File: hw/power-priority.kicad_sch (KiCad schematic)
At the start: 12 parts, among them IC1801 LM74800QDRRRQ1, Q1801 IPB026N06NATMA1, Q2307 IPB026N06NATMA1, Q2308 IPB026N06NATMA1, Q2309 2N7002, U2304 LM74700QDRQ1

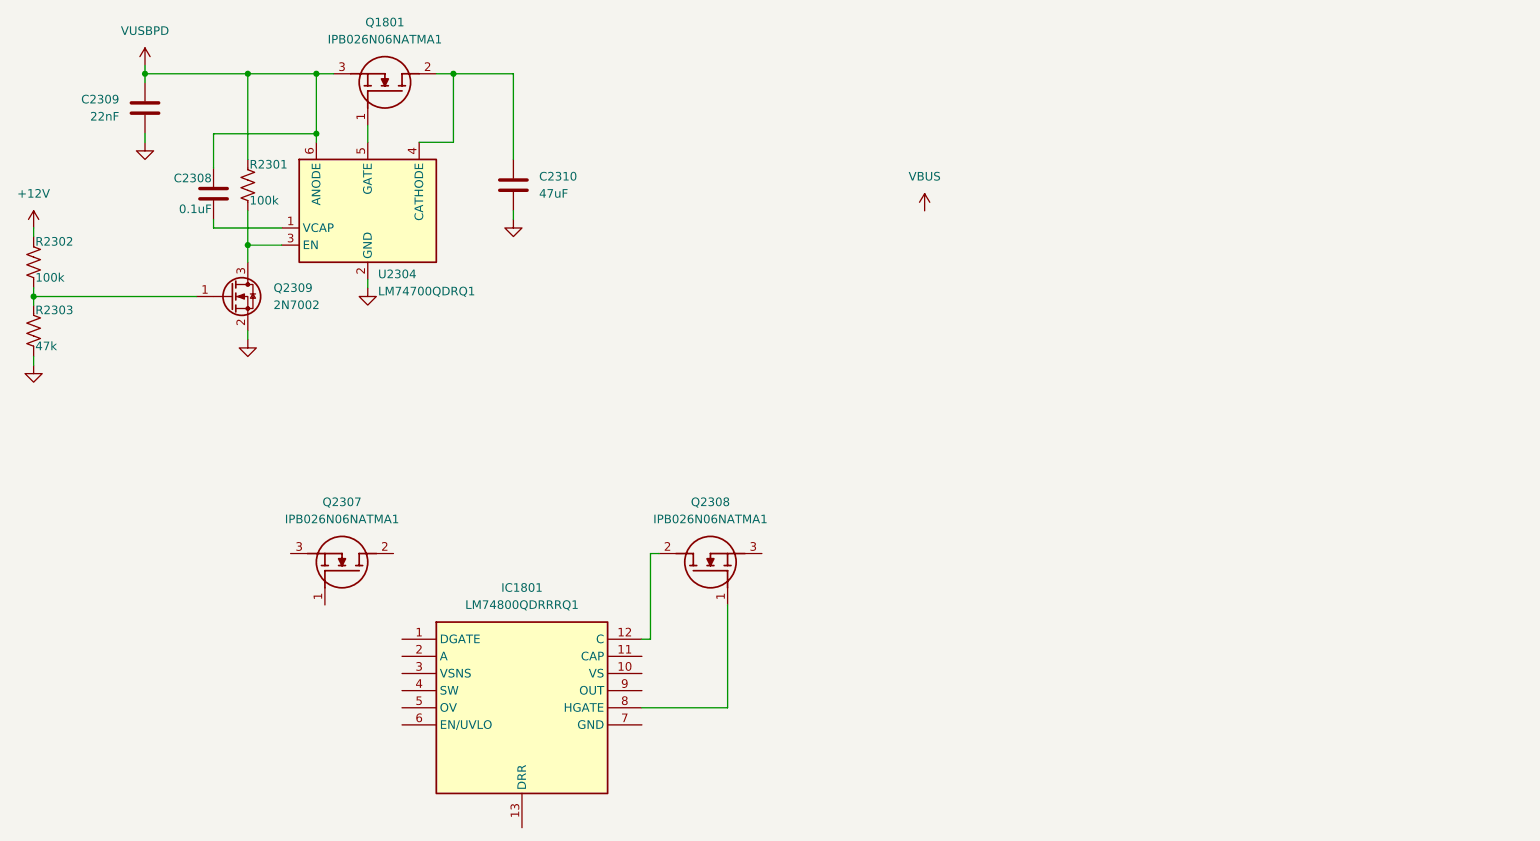
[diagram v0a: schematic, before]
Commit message: Schematic capture of the USBPD and +12V (+12V has priority) power scheme is "done". Have started working on RF deck mezzanine module but not yet divorced into another project
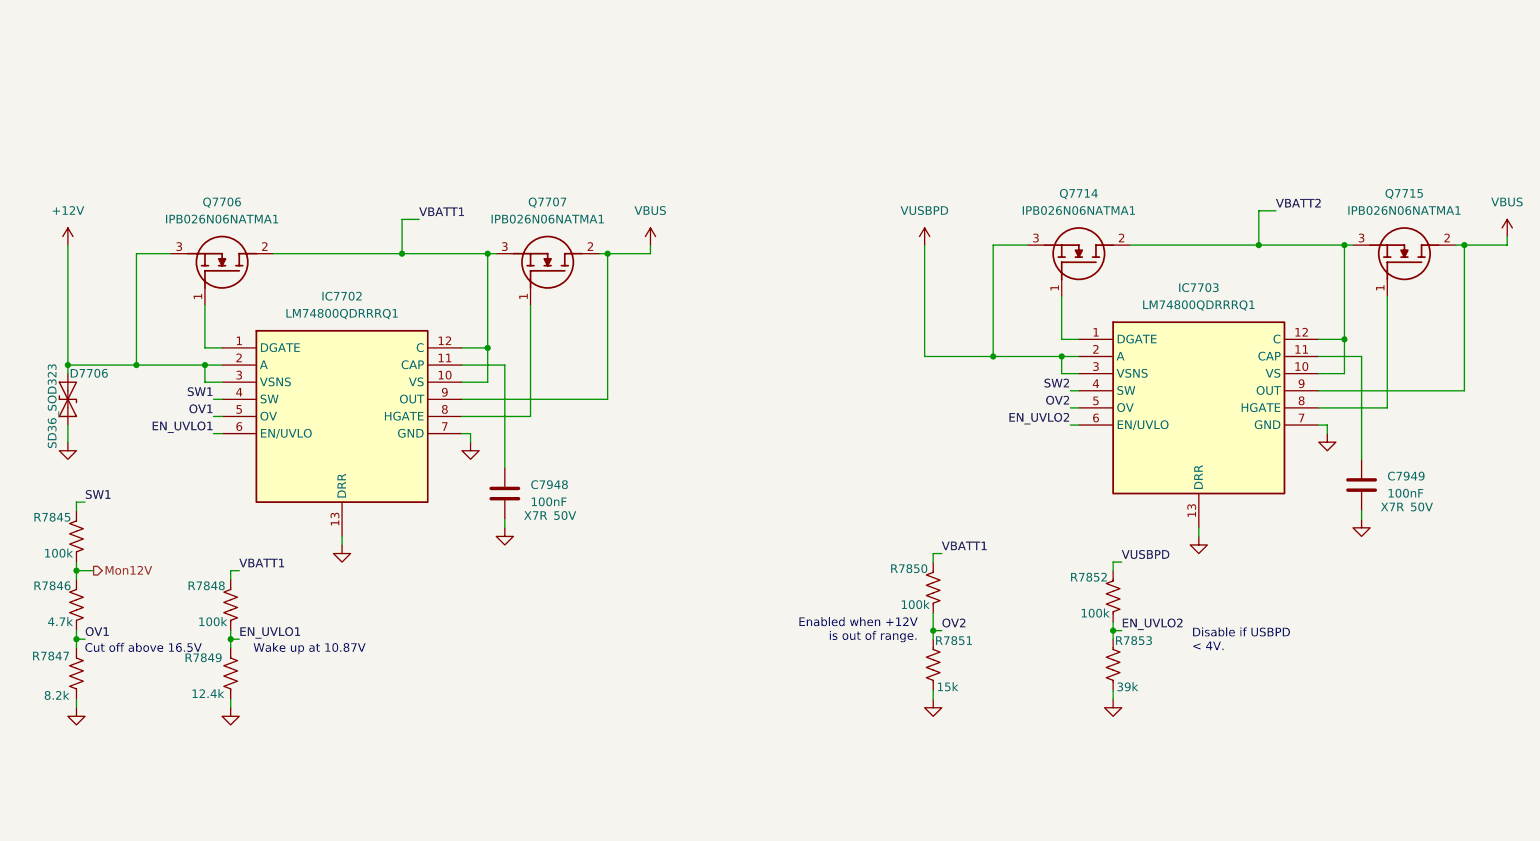
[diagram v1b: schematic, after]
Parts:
- removed C2308: 0.1uF, symbol Device:C
- removed C2309: 22nF, symbol Device:C
- removed C2310: 47uF, symbol Device:C
- removed Q1801, Q2308: IPB026N06NATMA1, IPB026N06NATMA1, symbol Library:IPB026N06NATMA1
- removed Q2309: 2N7002, Package_TO_SOT_SMD:SOT-23, symbol Transistor_FET:2N7002
- removed R2301, R2302: 100k, symbol Device:R_US
- removed R2303: 47k, symbol Device:R_US
- removed U2304: LM74700QDRQ1, Package_TO_SOT_SMD:SOT-23-6, symbol Power_Management:LM74700
- added C7948, C7949: 100nF, symbol Device:C
- added D7706: SD36_SOD323, Diode_SMD:D_SOD-323, symbol Diode:SD36_SOD323
- added IC7703: LM74800QDRRRQ1, SON50P300X300X80-13N, symbol Library:LM74800QDRRRQ1
- added Q7707, Q7714, Q7715: IPB026N06NATMA1, IPB026N06NATMA1, symbol Library:IPB026N06NATMA1
- added R7845, R7848, R7850, R7852: 100k, symbol Device:R_US
- added R7846: 4.7k, symbol Device:R_US
- added R7847: 8.2k, symbol Device:R_US
- added R7849: 12.4k, symbol Device:R_US
- added R7851: 15k, symbol Device:R_US
- added R7853: 39k, symbol Device:R_US
- renumbered IC1801 to IC7702, Q2307 to Q7706
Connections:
- net +12V: now also IC7702.2 (A), IC7702.3 (VSNS), Q7706.3 (S), D7706.2 (A2)
- net GND: now also IC7702.13 (DRR), IC7702.7 (GND), C7948.2, C7949.2, D7706.1 (A1), IC7703.13 (DRR), IC7703.7 (GND), R7847.2, R7849.2, R7851.2, R7853.2
- net VBUS: now also IC7702.9 (OUT), IC7703.9 (OUT), Q7707.2 (D), Q7715.2 (D)
- net VUSBPD: now also IC7703.2 (A), IC7703.3 (VSNS), Q7714.3 (S), R7852.1
- net at IC7702.8 (HGATE): now also Q7707.1 (G)
- net VBATT1: now reaches IC7702.12 (C)
- net VBATT1: now also IC7702.10 (VS), Q7706.2 (D), Q7707.3 (S), R7848.1, R7850.1
- net at IC7702.1 (DGATE): now also Q7706.1 (G)
- net at IC7702.11 (CAP): now also C7948.1
- net SW1: now reaches IC7702.4 (SW)
- net SW1: now also R7845.1
- net OV1: now reaches IC7702.5 (OV)
- net OV1: now also R7846.2, R7847.1
- net EN_UVLO1: now reaches IC7702.6 (EN/UVLO)
- net EN_UVLO1: now also R7848.2, R7849.1
- new net: IC7703.1 (DGATE), Q7714.1 (G)
- new net: C7949.1, IC7703.11 (CAP)
- new net: IC7703.8 (HGATE), Q7715.1 (G)
- new net EN_UVLO2: IC7703.6 (EN/UVLO), R7852.2, R7853.1
- new net Mon12V: R7845.2, R7846.1
- new net OV2: IC7703.5 (OV), R7850.2, R7851.1
- new net SW2: IC7703.4 (SW)
- new net VBATT2: IC7703.10 (VS), IC7703.12 (C), Q7714.2 (D), Q7715.3 (S)
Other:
- note added: "Cut off above 16.5V"
- note added: "Disable if USBPD < 4V."
- note added: "Enabled when +12V is out of range."
- note added: "Wake up at 10.87V"
- moved on the sheet: IC7702, Q7706

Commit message: Last rites for 800 ohm rx preselector, and probably the RF deck which was stillborn
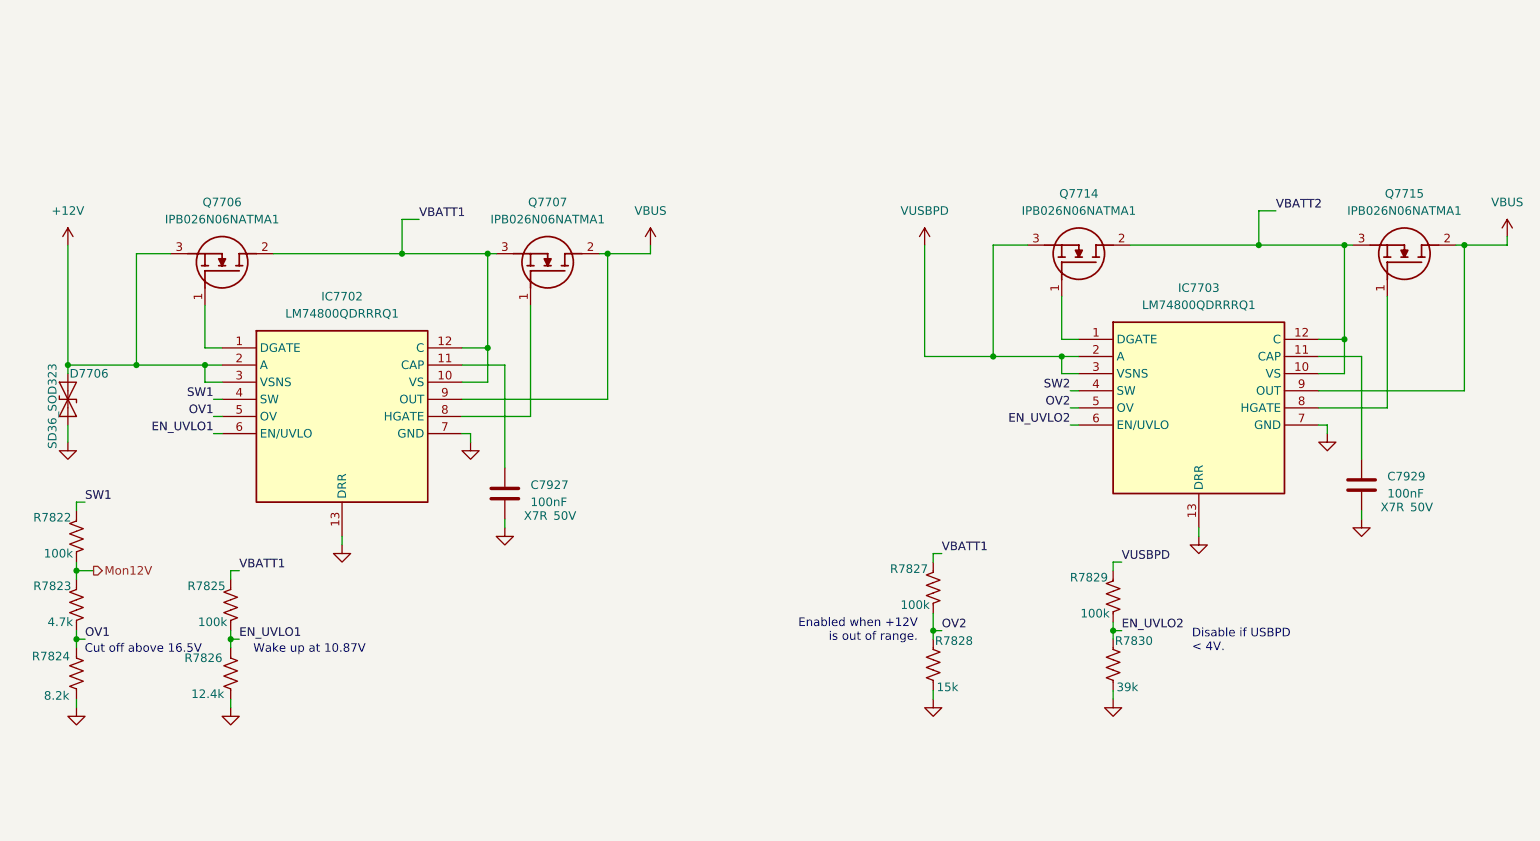
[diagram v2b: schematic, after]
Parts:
- renumbered C7948 to C7927, C7949 to C7929, R7845 to R7822, R7846 to R7823, R7847 to R7824, R7848 to R7825, R7849 to R7826, R7850 to R7827, R7851 to R7828, R7852 to R7829, R7853 to R7830
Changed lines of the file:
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@@
 	(title_block
 		(title "Power Priority Switching")
-		(date "2025-11-21")
+		(date "2025-10-13")
 		(company "WB7NAB")
 		(comment 1 "Alan Mimms")
@@
 		(dnp no)
 		(fields_autoplaced yes)
-		(property "Reference" "#PWR08038"
+		(property "Reference" "#PWR07982"
 			(at 127 72.39 0)
 			(effects
@@
 			(project "NexRig"
 				(path "/8ae46c04-d01a-4756-8774-512b694bfaff/cbf7569b-90aa-4e1a-84a7-d4153f6242b6/b06410ec-4c8e-4291-9691-3a63bcaba95c"
-					(reference "#PWR08038")
+					(reference "#PWR07982")
 					(unit 1)
 				)
@@
 		(dnp no)
 		(fields_autoplaced yes)
-		(property "Reference" "#PWR08034"
+		(property "Reference" "#PWR07978"
 			(at 100.33 104.14 0)
 			(effects
@@
 			(project "NexRig"
 				(path "/8ae46c04-d01a-4756-8774-512b694bfaff/cbf7569b-90aa-4e1a-84a7-d4153f6242b6/b06410ec-4c8e-4291-9691-3a63bcaba95c"
-					(reference "#PWR08034")
+					(reference "#PWR07978")
 					(unit 1)
 				)
@@
 		(on_board yes)
 		(dnp no)
-		(property "Reference" "R7853"
+		(property "Reference" "R7830"
 			(at 195.834 127.254 0)
 			(effects
@@
 			(project "NexRig"
 				(path "/8ae46c04-d01a-4756-8774-512b694bfaff/cbf7569b-90aa-4e1a-84a7-d4153f6242b6/b06410ec-4c8e-4291-9691-3a63bcaba95c"
-					(reference "R7853")
+					(reference "R7830")
 					(unit 1)
 				)
@@
 		(dnp no)
 		(fields_autoplaced yes)
-		(property "Reference" "#PWR08025"
+		(property "Reference" "#PWR07969"
 			(at 40.64 72.39 0)
 			(effects
@@
 			(project "NexRig"
 				(path "/8ae46c04-d01a-4756-8774-512b694bfaff/cbf7569b-90aa-4e1a-84a7-d4153f6242b6/b06410ec-4c8e-4291-9691-3a63bcaba95c"
-					(reference "#PWR08025")
+					(reference "#PWR07969")
 					(unit 1)
 				)
@@
 		(on_board yes)
 		(dnp no)
-		(property "Reference" "R7847"
+		(property "Reference" "R7824"
 			(at 35.306 129.54 0)
 			(effects
@@
 			(project ""
 				(path "/8ae46c04-d01a-4756-8774-512b694bfaff/cbf7569b-90aa-4e1a-84a7-d4153f6242b6/b06410ec-4c8e-4291-9691-3a63bcaba95c"
-					(reference "R7847")
+					(reference "R7824")
 					(unit 1)
 				)
@@
 		(dnp no)
 		(fields_autoplaced yes)
-		(property "Reference" "#PWR08043"
+		(property "Reference" "#PWR07987"
 			(at 167.64 72.39 0)
 			(effects
@@
 			(project "NexRig"
 				(path "/8ae46c04-d01a-4756-8774-512b694bfaff/cbf7569b-90aa-4e1a-84a7-d4153f6242b6/b06410ec-4c8e-4291-9691-3a63bcaba95c"
-					(reference "#PWR08043")
+					(reference "#PWR07987")
 					(unit 1)
 				)
@@
 		(on_board yes)
 		(dnp no)
-		(property "Reference" "R7848"
+		(property "Reference" "R7825"
 			(at 64.008 119.126 0)
 			(effects
@@
 			(project "NexRig"
 				(path "/8ae46c04-d01a-4756-8774-512b694bfaff/cbf7569b-90aa-4e1a-84a7-d4153f6242b6/b06410ec-4c8e-4291-9691-3a63bcaba95c"
-					(reference "R7848")
+					(reference "R7825")
 					(unit 1)
 				)
@@
 		(on_board yes)
 		(dnp no)
-		(property "Reference" "R7845"
+		(property "Reference" "R7822"
 			(at 41.148 108.966 0)
 			(effects
@@
 			(project "NexRig"
 				(path "/8ae46c04-d01a-4756-8774-512b694bfaff/cbf7569b-90aa-4e1a-84a7-d4153f6242b6/b06410ec-4c8e-4291-9691-3a63bcaba95c"
-					(reference "R7845")
+					(reference "R7822")
 					(unit 1)
 				)
@@
 		(on_board yes)
 		(dnp no)
-		(property "Reference" "R7850"
+		(property "Reference" "R7827"
 			(at 168.148 116.586 0)
 			(effects
@@
 			(project "NexRig"
 				(path "/8ae46c04-d01a-4756-8774-512b694bfaff/cbf7569b-90aa-4e1a-84a7-d4153f6242b6/b06410ec-4c8e-4291-9691-3a63bcaba95c"
-					(reference "R7850")
+					(reference "R7827")
 					(unit 1)
 				)
@@
 		(dnp no)
 		(fields_autoplaced yes)
-		(property "Reference" "#PWR08031"
+		(property "Reference" "#PWR07975"
 			(at 81.28 119.38 0)
 			(effects
@@
 			(project "NexRig"
 				(path "/8ae46c04-d01a-4756-8774-512b694bfaff/cbf7569b-90aa-4e1a-84a7-d4153f6242b6/b06410ec-4c8e-4291-9691-3a63bcaba95c"
-					(reference "#PWR08031")
+					(reference "#PWR07975")
 					(unit 1)
 				)
@@
 		(on_board yes)
 		(dnp no)
-		(property "Reference" "R7849"
+		(property "Reference" "R7826"
 			(at 57.912 129.794 0)
 			(effects
@@
 			(project "NexRig"
 				(path "/8ae46c04-d01a-4756-8774-512b694bfaff/cbf7569b-90aa-4e1a-84a7-d4153f6242b6/b06410ec-4c8e-4291-9691-3a63bcaba95c"
-					(reference "R7849")
+					(reference "R7826")
 					(unit 1)
 				)
@@
 		(dnp no)
 		(fields_autoplaced yes)
-		(property "Reference" "#PWR08051"
+		(property "Reference" "#PWR07994"
 			(at 227.33 102.87 0)
 			(effects
@@
 			(project "NexRig"
 				(path "/8ae46c04-d01a-4756-8774-512b694bfaff/cbf7569b-90aa-4e1a-84a7-d4153f6242b6/b06410ec-4c8e-4291-9691-3a63bcaba95c"
-					(reference "#PWR08051")
+					(reference "#PWR07994")
 					(unit 1)
 				)
@@
 		(dnp no)
 		(fields_autoplaced yes)
-		(property "Reference" "#PWR08047"
+		(property "Reference" "#PWR07991"
 			(at 208.28 118.11 0)
 			(effects
@@
 			(project "NexRig"
 				(path "/8ae46c04-d01a-4756-8774-512b694bfaff/cbf7569b-90aa-4e1a-84a7-d4153f6242b6/b06410ec-4c8e-4291-9691-3a63bcaba95c"
-					(reference "#PWR08047")
+					(reference "#PWR07991")
 					(unit 1)
 				)
@@
 		(dnp no)
 		(fields_autoplaced yes)
-		(property "Reference" "#PWR08026"
+		(property "Reference" "#PWR07970"
 			(at 40.64 104.14 0)
 			(effects
@@
 			(project "NexRig"
 				(path "/8ae46c04-d01a-4756-8774-512b694bfaff/cbf7569b-90aa-4e1a-84a7-d4153f6242b6/b06410ec-4c8e-4291-9691-3a63bcaba95c"
-					(reference "#PWR08026")
+					(reference "#PWR07970")
 					(unit 1)
 				)
@@
 		(on_board yes)
 		(dnp no)
-		(property "Reference" "R7852"
+		(property "Reference" "R7829"
 			(at 194.818 117.856 0)
 			(effects
@@
 			(project "NexRig"
 				(path "/8ae46c04-d01a-4756-8774-512b694bfaff/cbf7569b-90aa-4e1a-84a7-d4153f6242b6/b06410ec-4c8e-4291-9691-3a63bcaba95c"
-					(reference "R7852")
+					(reference "R7829")
 					(unit 1)
 				)
@@
 		(dnp no)
 		(fields_autoplaced yes)
-		(property "Reference" "#PWR08028"
+		(property "Reference" "#PWR07972"
 			(at 41.91 143.51 0)
 			(effects
@@
 			(project "NexRig"
 				(path "/8ae46c04-d01a-4756-8774-512b694bfaff/cbf7569b-90aa-4e1a-84a7-d4153f6242b6/b06410ec-4c8e-4291-9691-3a63bcaba95c"
-					(reference "#PWR08028")
+					(reference "#PWR07972")
 					(unit 1)
 				)
@@
 		(dnp no)
 		(fields_autoplaced yes)
-		(property "Reference" "#PWR08052"
+		(property "Reference" "#PWR07995"
 			(at 232.41 115.57 0)
 			(effects
@@
 			(project "NexRig"
 				(path "/8ae46c04-d01a-4756-8774-512b694bfaff/cbf7569b-90aa-4e1a-84a7-d4153f6242b6/b06410ec-4c8e-4291-9691-3a63bcaba95c"
-					(reference "#PWR08052")
+					(reference "#PWR07995")
 					(unit 1)
 				)
@@
 		(on_board yes)
 		(dnp no)
-		(property "Reference" "C7949"
+		(property "Reference" "C7929"
 			(at 236.22 102.8699 0)
 			(effects
@@
 			(project "NexRig"
 				(path "/8ae46c04-d01a-4756-8774-512b694bfaff/cbf7569b-90aa-4e1a-84a7-d4153f6242b6/b06410ec-4c8e-4291-9691-3a63bcaba95c"
-					(reference "C7949")
+					(reference "C7929")
 					(unit 1)
 				)
@@
 		(dnp no)
 		(fields_autoplaced yes)
-		(property "Reference" "#PWR08030"
+		(property "Reference" "#PWR07974"
 			(at 64.77 143.51 0)
 			(effects
@@
 			(project "NexRig"
 				(path "/8ae46c04-d01a-4756-8774-512b694bfaff/cbf7569b-90aa-4e1a-84a7-d4153f6242b6/b06410ec-4c8e-4291-9691-3a63bcaba95c"
-					(reference "#PWR08030")
+					(reference "#PWR07974")
 					(unit 1)
 				)
@@
 		(dnp no)
 		(fields_autoplaced yes)
-		(property "Reference" "#PWR08054"
+		(property "Reference" "#PWR07998"
 			(at 254 71.12 0)
 			(effects
@@
 			(project "NexRig"
 				(path "/8ae46c04-d01a-4756-8774-512b694bfaff/cbf7569b-90aa-4e1a-84a7-d4153f6242b6/b06410ec-4c8e-4291-9691-3a63bcaba95c"
-					(reference "#PWR08054")
+					(reference "#PWR07998")
 					(unit 1)
 				)
@@
 		(dnp no)
 		(fields_autoplaced yes)
-		(property "Reference" "#PWR08035"
+		(property "Reference" "#PWR07979"
 			(at 105.41 116.84 0)
 			(effects
@@
 			(project "NexRig"
 				(path "/8ae46c04-d01a-4756-8774-512b694bfaff/cbf7569b-90aa-4e1a-84a7-d4153f6242b6/b06410ec-4c8e-4291-9691-3a63bcaba95c"
-					(reference "#PWR08035")
+					(reference "#PWR07979")
 					(unit 1)
 				)
@@
 		(dnp no)
 		(fields_autoplaced yes)
-		(property "Reference" "#PWR08046"
+		(property "Reference" "#PWR07990"
 			(at 195.58 142.24 0)
 			(effects
@@
 			(project "NexRig"
 				(path "/8ae46c04-d01a-4756-8774-512b694bfaff/cbf7569b-90aa-4e1a-84a7-d4153f6242b6/b06410ec-4c8e-4291-9691-3a63bcaba95c"
-					(reference "#PWR08046")
+					(reference "#PWR07990")
 					(unit 1)
 				)
@@
 		(on_board yes)
 		(dnp no)
-		(property "Reference" "R7851"
+		(property "Reference" "R7828"
 			(at 169.164 127.254 0)
 			(effects
@@
 			(project "NexRig"
 				(path "/8ae46c04-d01a-4756-8774-512b694bfaff/cbf7569b-90aa-4e1a-84a7-d4153f6242b6/b06410ec-4c8e-4291-9691-3a63bcaba95c"
-					(reference "R7851")
+					(reference "R7828")
 					(unit 1)
 				)
@@
 		(dnp no)
 		(fields_autoplaced yes)
-		(property "Reference" "#PWR08044"
+		(property "Reference" "#PWR07988"
 			(at 168.91 142.24 0)
 			(effects
@@
 			(project "NexRig"
 				(path "/8ae46c04-d01a-4756-8774-512b694bfaff/cbf7569b-90aa-4e1a-84a7-d4153f6242b6/b06410ec-4c8e-4291-9691-3a63bcaba95c"
-					(reference "#PWR08044")
+					(reference "#PWR07988")
 					(unit 1)
 				)
@@
 		(on_board yes)
 		(dnp no)
-		(property "Reference" "C7948"
+		(property "Reference" "C7927"
 			(at 109.22 104.1399 0)
 			(effects
@@
 			(project "NexRig"
 				(path "/8ae46c04-d01a-4756-8774-512b694bfaff/cbf7569b-90aa-4e1a-84a7-d4153f6242b6/b06410ec-4c8e-4291-9691-3a63bcaba95c"
-					(reference "C7948")
+					(reference "C7927")
 					(unit 1)
 				)
@@
 		(on_board yes)
 		(dnp no)
-		(property "Reference" "R7846"
+		(property "Reference" "R7823"
 			(at 41.148 119.126 0)
 			(effects
@@
 			(project "NexRig"
 				(path "/8ae46c04-d01a-4756-8774-512b694bfaff/cbf7569b-90aa-4e1a-84a7-d4153f6242b6/b06410ec-4c8e-4291-9691-3a63bcaba95c"
-					(reference "R7846")
+					(reference "R7823")
 					(unit 1)
 				)
